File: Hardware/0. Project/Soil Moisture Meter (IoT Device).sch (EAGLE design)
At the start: 22 parts, among them J1 ICSP, Q1 32.768 kHz, U1 MSP430FR4133

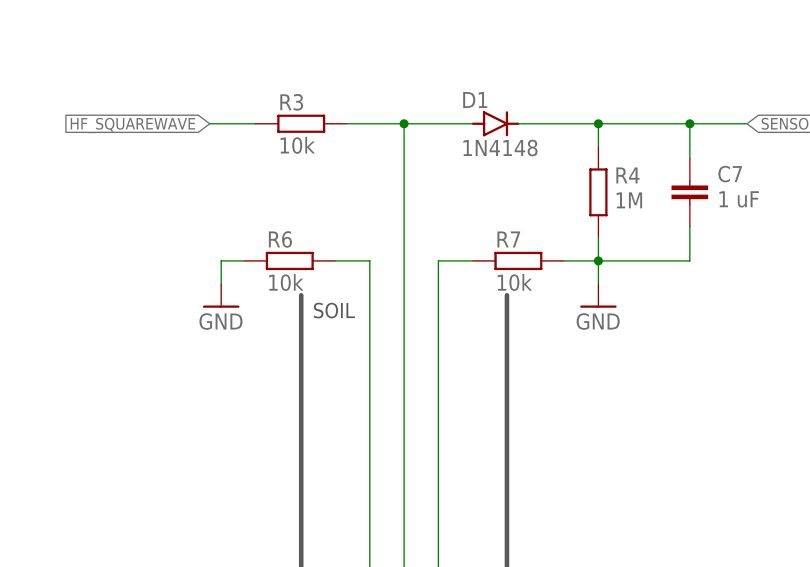
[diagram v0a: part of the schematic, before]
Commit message: Changed folder structure
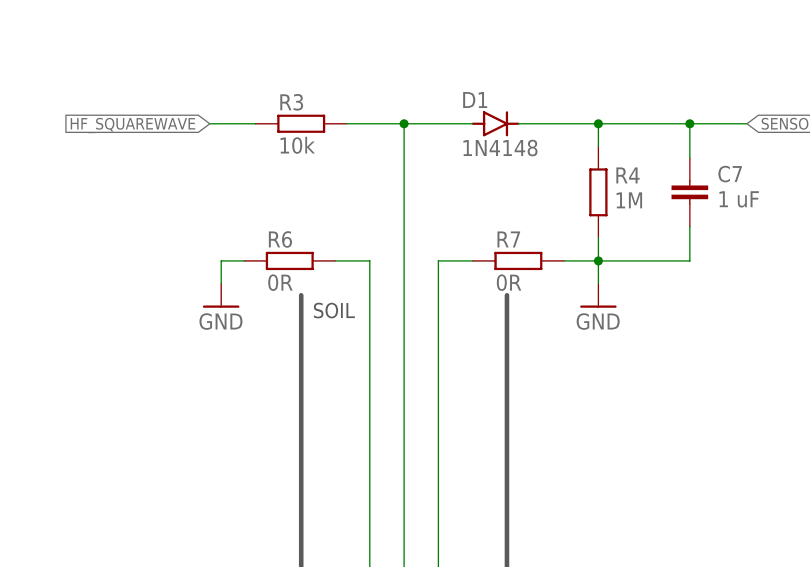
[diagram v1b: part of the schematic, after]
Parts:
- R6, R7: value 10k -> 0R
